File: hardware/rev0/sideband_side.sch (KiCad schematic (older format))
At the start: 10 parts, among them IC1 ECP5-BGA256, U8 USB3343

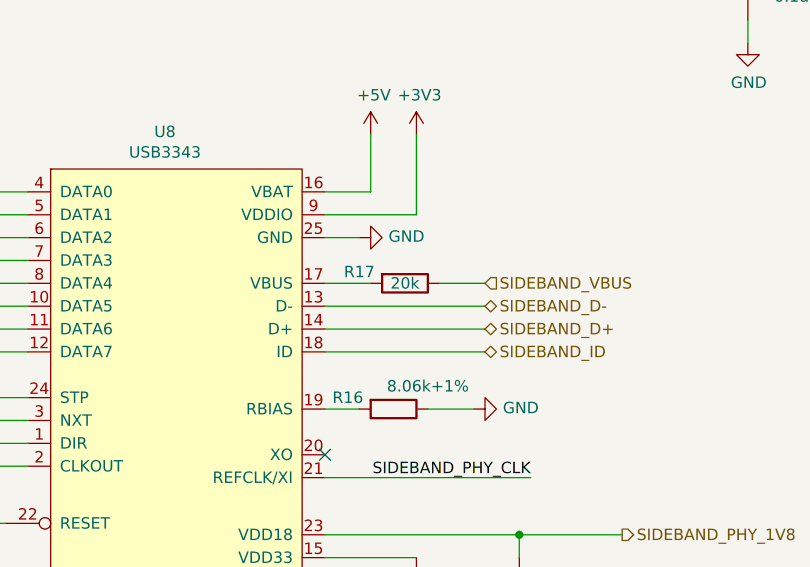
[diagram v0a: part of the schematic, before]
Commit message: hardware: add part numbers
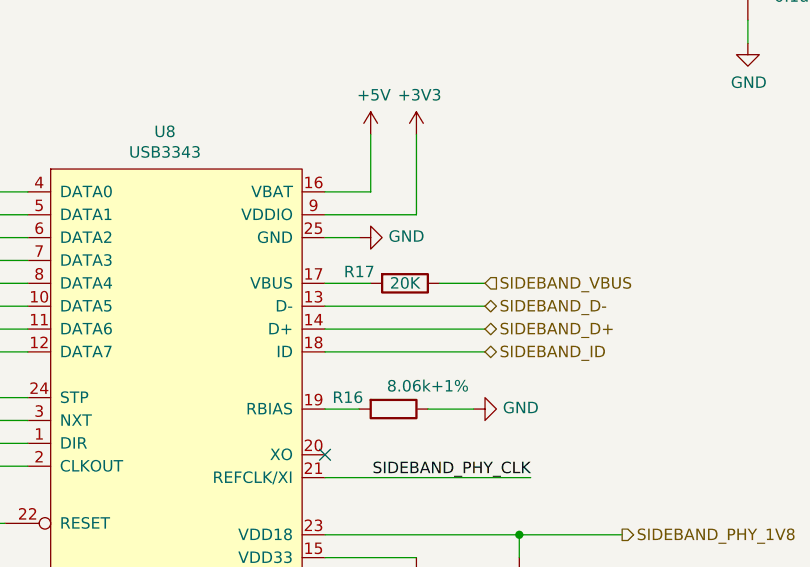
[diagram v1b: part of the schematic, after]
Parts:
- C36, C37: Manufacturer_Part_Number (none) -> GENERIC-CAP-0603-1uF
- R15: Manufacturer_Part_Number (none) -> GENERIC-RES-0402-1K
- R16: Description (none) -> RES SMD 8.06K OHM 1% 1/10W 0402; Manufacturer_Name (none) -> Panasonic; Manufacturer_Part_Number (none) -> ERJ-2RKF8061X
- R17: value 20k -> 20K; Description (none) -> RES 20K OHM 0.1% 1/16W 0402; Manufacturer_Name (none) -> TE Connectivity; Manufacturer_Part_Number (none) -> RP73PF1E20KBTDF
- R22: Manufacturer_Part_Number (none) -> GENERIC-RES-0402-15K
- U8: Description (none) -> IC TRANSCEIVER 1/1 24QFN; Manufacturer_Name (none) -> Microchip; Manufacturer_Part_Number (none) -> USB3343-CP
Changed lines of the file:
@@
 EESchema Schematic File Version 4
-LIBS:luna_rev0-cache
 EELAYER 30 0
 EELAYER END
@@
 F 2 "Package_DFN_QFN:VQFN-24-1EP_4x4mm_P0.5mm_EP2.45x2.45mm" H 5450 2350 50  0001 C CNN
 F 3 "http://ww1.microchip.com/downloads/en/DeviceDoc/334x.pdf" H 5450 2350 50  0001 C CNN
+F 4 "IC TRANSCEIVER 1/1 24QFN" H 5450 2350 50  0001 C CNN "Description"
+F 5 "Microchip" H 5450 2350 50  0001 C CNN "Manufacturer_Name"
+F 6 "USB3343-CP" H 5450 2350 50  0001 C CNN "Manufacturer_Part_Number"
 	1    5450 2350
 	1    0    0    -1
@@
 F 2 "Capacitor_SMD:C_0603_1608Metric" H 7188 4050 50  0001 C CNN
 F 3 "~" H 7150 4200 50  0001 C CNN
+F 4 "GENERIC-CAP-0603-1uF" H 7150 4200 50  0001 C CNN "Manufacturer_Part_Number"
 	1    7150 4200
 	1    0    0    -1
@@
 F 2 "Capacitor_SMD:C_0603_1608Metric" H 7638 4050 50  0001 C CNN
 F 3 "~" H 7600 4200 50  0001 C CNN
+F 4 "GENERIC-CAP-0603-1uF" H 7600 4200 50  0001 C CNN "Manufacturer_Part_Number"
 	1    7600 4200
 	1    0    0    -1
@@
 F 2 "Resistor_SMD:R_0402_1005Metric" V 6980 3400 50  0001 C CNN
 F 3 "~" H 7050 3400 50  0001 C CNN
+F 4 "RES SMD 8.06K OHM 1% 1/10W 0402" H 7050 3400 50  0001 C CNN "Description"
+F 5 "Panasonic" H 7050 3400 50  0001 C CNN "Manufacturer_Name"
+F 6 "ERJ-2RKF8061X" H 7050 3400 50  0001 C CNN "Manufacturer_Part_Number"
 	1    7050 3400
 	0    1    1    0
@@
 P 7100 2850
 F 0 "R17" V 7050 2650 50  0000 C CNN
-F 1 "20k" V 7100 2850 50  0000 C CNN
+F 1 "20K" V 7100 2850 50  0000 C CNN
 F 2 "Resistor_SMD:R_0402_1005Metric" V 7030 2850 50  0001 C CNN
 F 3 "~" H 7100 2850 50  0001 C CNN
+F 4 "RES 20K OHM 0.1% 1/16W 0402" H 7100 2850 50  0001 C CNN "Description"
+F 5 "TE Connectivity" H 7100 2850 50  0001 C CNN "Manufacturer_Name"
+F 6 "RP73PF1E20KBTDF" H 7100 2850 50  0001 C CNN "Manufacturer_Part_Number"
 	1    7100 2850
 	0    1    1    0
@@
 F 2 "Resistor_SMD:R_0402_1005Metric" V 2880 5350 50  0001 C CNN
 F 3 "~" H 2950 5350 50  0001 C CNN
+F 4 "GENERIC-RES-0402-1K" H 2950 5350 50  0001 C CNN "Manufacturer_Part_Number"
 	1    2950 5350
 	0    1    1    0
@@
 F 2 "Resistor_SMD:R_0402_1005Metric" V 4830 4600 50  0001 C CNN
 F 3 "~" H 4900 4600 50  0001 C CNN
+F 4 "GENERIC-RES-0402-15K" H 4900 4600 50  0001 C CNN "Manufacturer_Part_Number"
 	1    4900 4600
 	-1   0    0    1

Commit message: hardware: normalize BOM fields
make compatible with kicad-bom-scripts
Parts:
- C36, C37: Manufacturer_Part_Number GENERIC-CAP-0603-1uF -> (none); Part Number (none) -> GENERIC-CAP-0603-1uF
- C38, C39: Part Number (none) -> GENERIC-CAP-0402-0.1uF
- IC1: Height 1.7 -> (none); Manufacturer (none) -> Lattice; Manufacturer_Name Lattice -> (none); Manufacturer_Part_Number LFE5U-12F-6BG256C -> (none); Mouser Part Number 842-LFE5U12F6BG256C -> (none); Mouser Price/Stock https://www.mouser.com/Search/Refine.aspx?Keyword=842-LFE5U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 -> (none); Part Number (none) -> LFE5U-12F-6BG256C
- R15: Manufacturer_Part_Number GENERIC-RES-0402-1K -> (none); Part Number (none) -> GENERIC-RES-0402-1K
- R16: Manufacturer (none) -> Panasonic; Manufacturer_Name Panasonic -> (none); Manufacturer_Part_Number ERJ-2RKF8061X -> (none); Part Number (none) -> ERJ-2RKF8061X
- R17: Manufacturer (none) -> TE Connectivity; Manufacturer_Name TE Connectivity -> (none); Manufacturer_Part_Number RP73PF1E20KBTDF -> (none); Part Number (none) -> RP73PF1E20KBTDF
- R22: Manufacturer_Part_Number GENERIC-RES-0402-15K -> (none); Part Number (none) -> GENERIC-RES-0402-15K
- U8: Manufacturer (none) -> Microchip; Manufacturer_Name Microchip -> (none); Manufacturer_Part_Number USB3343-CP -> (none); Part Number (none) -> USB3343-CP
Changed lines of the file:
@@
 F 3 "http://ww1.microchip.com/downloads/en/DeviceDoc/334x.pdf" H 5450 2350 50  0001 C CNN
 F 4 "IC TRANSCEIVER 1/1 24QFN" H 5450 2350 50  0001 C CNN "Description"
-F 5 "Microchip" H 5450 2350 50  0001 C CNN "Manufacturer_Name"
-F 6 "USB3343-CP" H 5450 2350 50  0001 C CNN "Manufacturer_Part_Number"
+F 5 "Microchip" H 5450 2350 50  0001 C CNN "Manufacturer"
+F 6 "USB3343-CP" H 5450 2350 50  0001 C CNN "Part Number"
 	1    5450 2350
 	1    0    0    -1
@@
 F 3 "" H -2100 6300 50  0001 L CNN
 F 4 "FPGA - Field Programmable Gate Array ECP5; 12k LUTs; 1.1V" H -2100 6200 50  0001 L CNN "Description"
-F 5 "1.7" H -2100 6550 50  0001 L CNN "Height"
-F 6 "Lattice" H -2050 7150 50  0001 L CNN "Manufacturer_Name"
-F 7 "LFE5U-12F-6BG256C" H -2050 7050 50  0001 L CNN "Manufacturer_Part_Number"
-F 8 "842-LFE5U12F6BG256C" H -1400 5750 50  0001 L CNN "Mouser Part Number"
-F 9 "https://www.mouser.com/Search/Refine.aspx?Keyword=842-LFE5U12F6BG256C" H -1750 5600 50  0001 L CNN "Mouser Price/Stock"
+F 5 "Lattice" H -2050 7150 50  0001 L CNN "Manufacturer"
+F 6 "LFE5U-12F-6BG256C" H -2050 7050 50  0001 L CNN "Part Number"
 	6    1550 1900
 	1    0    0    -1
@@
 F 2 "Capacitor_SMD:C_0603_1608Metric" H 7188 4050 50  0001 C CNN
 F 3 "~" H 7150 4200 50  0001 C CNN
-F 4 "GENERIC-CAP-0603-1uF" H 7150 4200 50  0001 C CNN "Manufacturer_Part_Number"
+F 4 "GENERIC-CAP-0603-1uF" H 7150 4200 50  0001 C CNN "Part Number"
 	1    7150 4200
 	1    0    0    -1
@@
 F 2 "Capacitor_SMD:C_0603_1608Metric" H 7638 4050 50  0001 C CNN
 F 3 "~" H 7600 4200 50  0001 C CNN
-F 4 "GENERIC-CAP-0603-1uF" H 7600 4200 50  0001 C CNN "Manufacturer_Part_Number"
+F 4 "GENERIC-CAP-0603-1uF" H 7600 4200 50  0001 C CNN "Part Number"
 	1    7600 4200
 	1    0    0    -1
@@
 F 3 "~" H 7050 3400 50  0001 C CNN
 F 4 "RES SMD 8.06K OHM 1% 1/10W 0402" H 7050 3400 50  0001 C CNN "Description"
-F 5 "Panasonic" H 7050 3400 50  0001 C CNN "Manufacturer_Name"
-F 6 "ERJ-2RKF8061X" H 7050 3400 50  0001 C CNN "Manufacturer_Part_Number"
+F 5 "Panasonic" H 7050 3400 50  0001 C CNN "Manufacturer"
+F 6 "ERJ-2RKF8061X" H 7050 3400 50  0001 C CNN "Part Number"
 	1    7050 3400
 	0    1    1    0
@@
 F 3 "~" H 7100 2850 50  0001 C CNN
 F 4 "RES 20K OHM 0.1% 1/16W 0402" H 7100 2850 50  0001 C CNN "Description"
-F 5 "TE Connectivity" H 7100 2850 50  0001 C CNN "Manufacturer_Name"
-F 6 "RP73PF1E20KBTDF" H 7100 2850 50  0001 C CNN "Manufacturer_Part_Number"
+F 5 "TE Connectivity" H 7100 2850 50  0001 C CNN "Manufacturer"
+F 6 "RP73PF1E20KBTDF" H 7100 2850 50  0001 C CNN "Part Number"
 	1    7100 2850
 	0    1    1    0
@@
 F 2 "Capacitor_SMD:C_0402_1005Metric" H 8638 1400 50  0001 C CNN
 F 3 "~" H 8600 1550 50  0001 C CNN
+F 4 "GENERIC-CAP-0402-0.1uF" H 8600 1550 50  0001 C CNN "Part Number"
 	1    8600 1550
 	1    0    0    -1
@@
 F 2 "Capacitor_SMD:C_0402_1005Metric" H 9138 1400 50  0001 C CNN
 F 3 "~" H 9100 1550 50  0001 C CNN
+F 4 "GENERIC-CAP-0402-0.1uF" H 9100 1550 50  0001 C CNN "Part Number"
 	1    9100 1550
 	1    0    0    -1
@@
 F 2 "Resistor_SMD:R_0402_1005Metric" V 2880 5350 50  0001 C CNN
 F 3 "~" H 2950 5350 50  0001 C CNN
-F 4 "GENERIC-RES-0402-1K" H 2950 5350 50  0001 C CNN "Manufacturer_Part_Number"
+F 4 "GENERIC-RES-0402-1K" H 2950 5350 50  0001 C CNN "Part Number"
 	1    2950 5350
 	0    1    1    0
@@
 F 2 "Resistor_SMD:R_0402_1005Metric" V 4830 4600 50  0001 C CNN
 F 3 "~" H 4900 4600 50  0001 C CNN
-F 4 "GENERIC-RES-0402-15K" H 4900 4600 50  0001 C CNN "Manufacturer_Part_Number"
+F 4 "GENERIC-RES-0402-15K" H 4900 4600 50  0001 C CNN "Part Number"
 	1    4900 4600
 	-1   0    0    1
